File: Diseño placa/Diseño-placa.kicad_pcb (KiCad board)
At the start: 2 copper layers, 57.1 x 44.4 mm, 89 parts, among them IC1 ATMEGA32-P, M1 DIL24, M2 DIL24, M3 DIL16, P1 CONN_01X03, P2 CONN_02X08, P3 CONN_01X01, P4 CONN_01X16, P5 CONN_01X05, P6 CONN_01X05, P7 CONN_02X03, SW1 SW_PUSH, SW2 SW_PUSH, SW3 SW_PUSH, SW4 SW_PUSH, SW5 SW_PUSH, U1 REG104, U2 OPA625, U3 OPA625, U4 OPA625, U5 OPA625, U6 OPA625, U7 OPA625, X1 16M

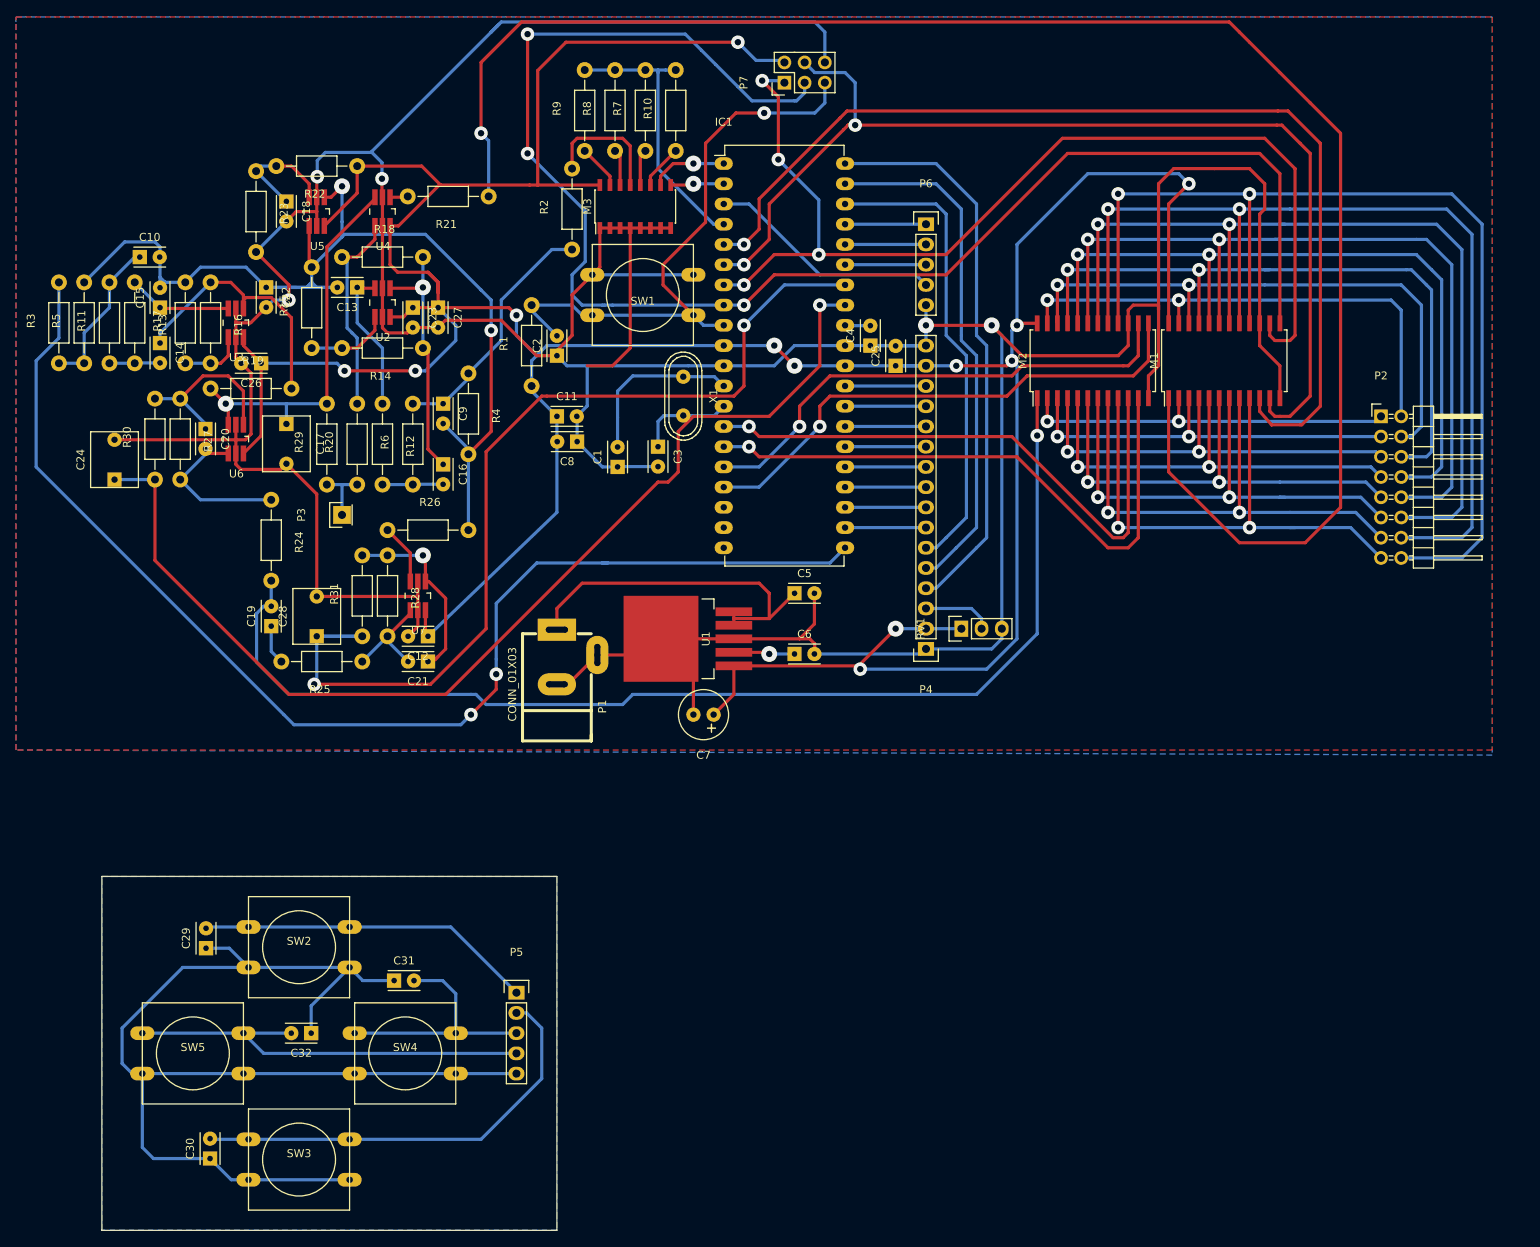
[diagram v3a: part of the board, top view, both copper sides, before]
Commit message: Corrección tamaño de capacitores
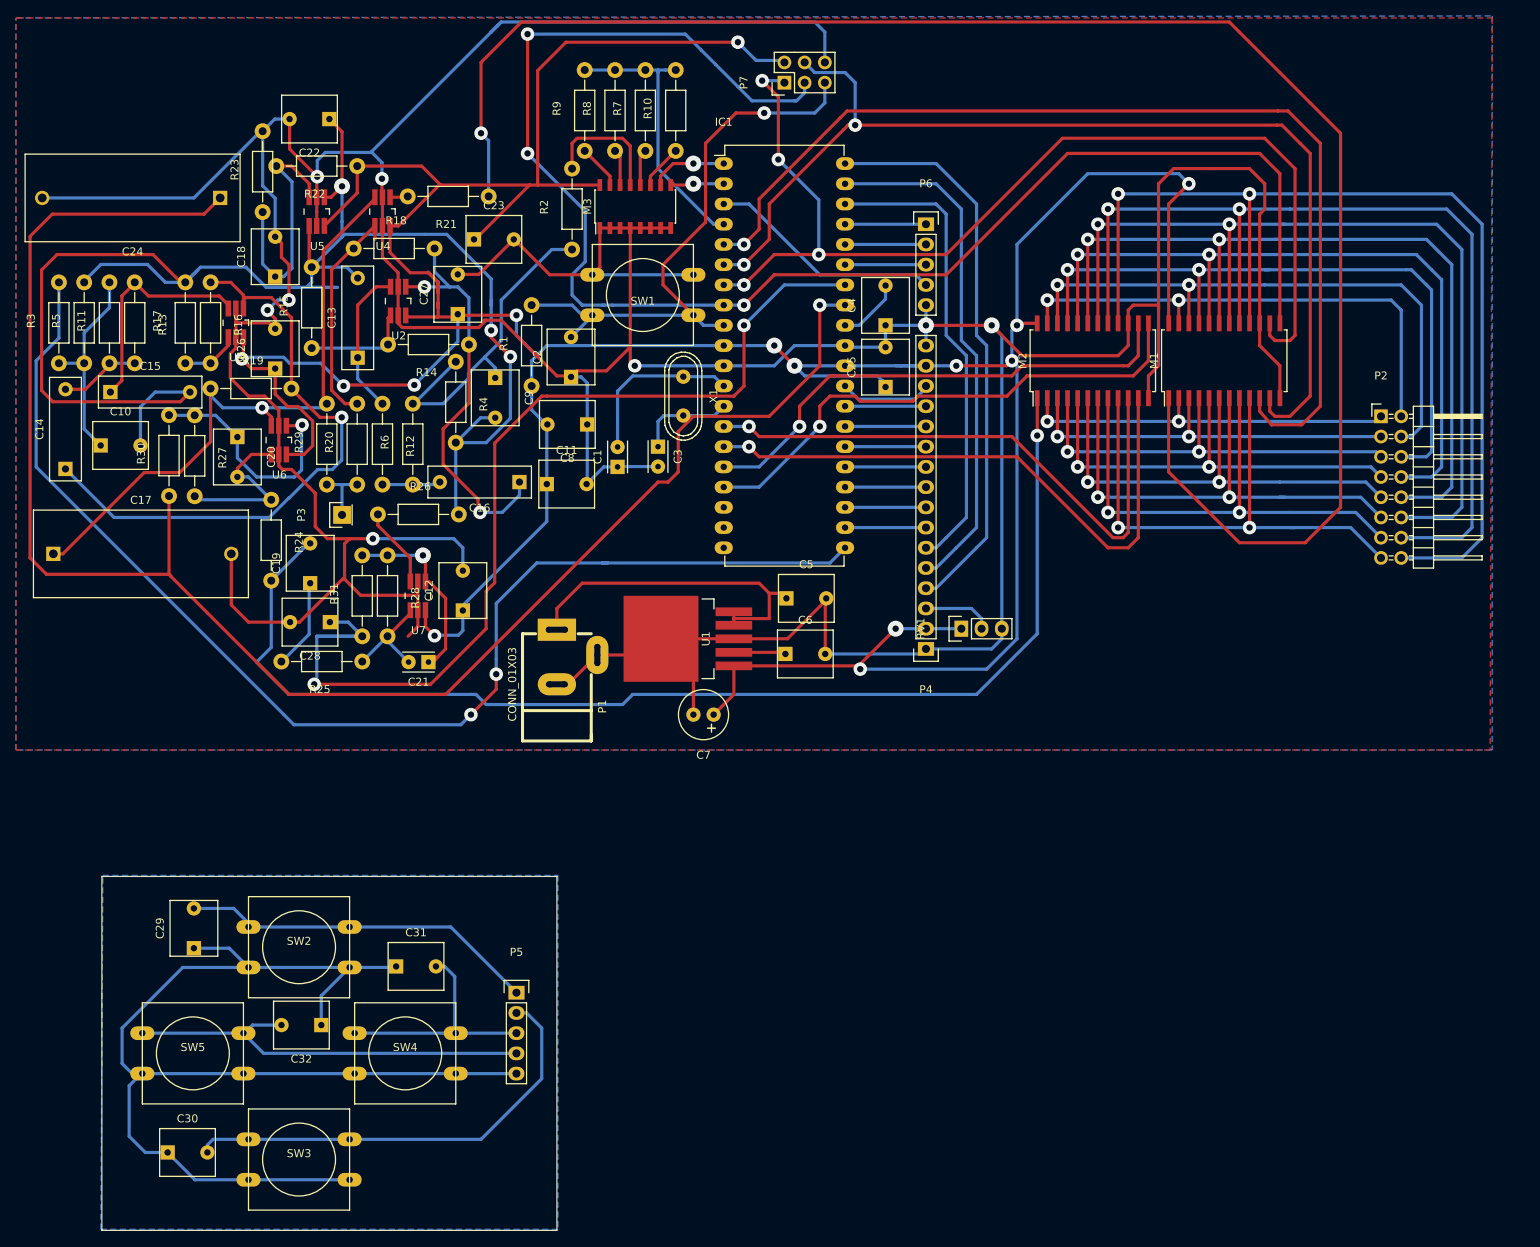
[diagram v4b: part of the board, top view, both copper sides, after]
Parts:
- C10, C11, C12, C18, C19, C2, C20, C22, C23, C25, C26, C27, C29, C30, C31, C32, C4, C5, C6, C8, C9: footprint Capacitors_ThroughHole:C_Rect_L4_W2.5_P2.5 -> Capacitors_ThroughHole:C_Rect_L7_W6_P5
- C13, C14, C15, C16: footprint Capacitors_ThroughHole:C_Rect_L4_W2.5_P2.5 -> Capacitors_ThroughHole:C_Rect_L13_W4_P10
- C17, C24: footprint Capacitors_ThroughHole:C_Rect_L7_W6_P5 -> Capacitors_ThroughHole:C_Rect_L27_W11_P22
- moved C24 37.8 mm to (54.9, 48.8), turned to 180 degrees
- moved C17 33.5 mm to (33.9, 93.5), turned to 0 degrees
- moved C10 24.2 mm to (39.9, 79.9)
- moved C22 22.6 mm to (68.6, 38.9), turned to 180 degrees
- moved C14 19.8 mm to (35.4, 82.8), turned to 90 degrees
- moved C15 12.3 mm to (41.1, 73.2), turned to 0 degrees
- moved C23 11.5 mm to (86.7, 54.0), turned to 0 degrees
- moved C16 9.84 mm to (92.5, 84.5), turned to 180 degrees
- moved C18 9.54 mm to (61.8, 58.6), turned to 90 degrees
- moved C13 8.83 mm to (72.1, 68.8), turned to 90 degrees
- moved C11 8.60 mm to (95.9, 84.7)
- moved C9 7.30 mm to (89.4, 71.4)
- moved C19 7.28 mm to (66.2, 97.2)
- moved R14 5.80 mm to (81.0, 67.2)
- moved C12 5.45 mm to (85.3, 100.6), turned to 90 degrees
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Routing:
- net /VCC/2: track 135.3 -> 217.5 mm, vias 2 -> 3
- net /GND: track 757.8 -> 838.7 mm, vias 5 -> 8
- net /ADCOFFSET: track 136.6 -> 213.3 mm
- net Net-(C14-Pad1): track 33.9 -> 77.0 mm, vias 0 -> 1
- net /VCC: track 456.9 -> 489.7 mm, vias 12 -> 14
- net /OFFSET: track 49.1 -> 80.4 mm
- net Net-(C16-Pad1): track 31.3 -> 51.8 mm, vias 1 -> 2
- net Net-(C18-Pad1): track 14.9 -> 31.7 mm
- net Net-(C15-Pad1): track 13.1 -> 28.4 mm
- net Net-(C9-Pad1): track 31.4 -> 42.1 mm
- net Net-(C20-Pad1): track 22.4 -> 29.5 mm, vias 0 -> 1
- net Net-(C19-Pad1): track 4.97 -> 11.4 mm
- net /MUX1IO: track 145.1 -> 151.3 mm
- net Net-(C10-Pad1): track 19.8 -> 25.8 mm
- net Net-(C4-Pad2): track 3.19 -> 8.20 mm
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
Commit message: Última versión PCB
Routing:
- net /VCC/2: track 217.5 -> 218.5 mm
- net Net-(R14-Pad2): track 13.6 -> 14.2 mm
- net /VCC: track 489.7 -> 490.3 mm
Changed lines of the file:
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@@
     (links 287)
     (no_connects 21)
-    (area 29.109999 25.934999 272.537601 178.485001)
+    (area 29.109999 25.908 272.537601 178.485001)
     (thickness 1.6)
     (drawings 10)
-    (tracks 1118)
+    (tracks 1136)
     (zones 0)
     (modules 89)
@@
   (segment (start 119.38 105.84) (end 125.652 105.84) (width 0.4) (layer F.Cu) (net 7))
   (segment (start 125.652 105.84) (end 125.857 106.045) (width 0.4) (layer F.Cu) (net 7))
+  (segment (start 96.266 67.31) (end 97.028 67.31) (width 0.4) (layer B.Cu) (net 8))
+  (segment (start 100.838 68.072) (end 101.6 67.31) (width 0.4) (layer B.Cu) (net 8))
+  (segment (start 97.79 68.072) (end 100.838 68.072) (width 0.4) (layer B.Cu) (net 8))
+  (segment (start 97.028 67.31) (end 97.79 68.072) (width 0.4) (layer B.Cu) (net 8))
   (segment (start 63.35395 74.97445) (end 64.66205 74.97445) (width 0.4) (layer F.Cu) (net 8))
   (segment (start 64.66205 74.97445) (end 66.4845 76.7969) (width 0.4) (layer F.Cu) (net 8))
@@
   (segment (start 93.98 72.39) (end 93.98 69.215) (width 0.4) (layer B.Cu) (net 8))
   (segment (start 93.98 69.215) (end 94.615 68.58) (width 0.4) (layer B.Cu) (net 8))
-  (segment (start 95.885 67.31) (end 118.11 67.31) (width 0.4) (layer B.Cu) (net 8))
+  (segment (start 95.885 67.31) (end 96.266 67.31) (width 0.4) (layer B.Cu) (net 8))
+  (segment (start 101.6 67.31) (end 118.11 67.31) (width 0.4) (layer B.Cu) (net 8))
   (segment (start 94.615 68.58) (end 95.885 67.31) (width 0.4) (layer B.Cu) (net 8))
   (segment (start 143.51 69.85) (end 139.7 69.85) (width 0.4) (layer B.Cu) (net 8))
@@
   (segment (start 86.0425 70.8025) (end 86.0425 71.4375) (width 0.4) (layer B.Cu) (net 9))
   (segment (start 86.0425 71.4375) (end 82.8675 74.6125) (width 0.4) (layer B.Cu) (net 9))
+  (segment (start 38.354 74.3712) (end 38.8112 74.3712) (width 0.4) (layer F.Cu) (net 10))
+  (segment (start 42.926 75.692) (end 44.2468 74.3712) (width 0.4) (layer F.Cu) (net 10))
+  (segment (start 40.132 75.692) (end 42.926 75.692) (width 0.4) (layer F.Cu) (net 10))
+  (segment (start 38.8112 74.3712) (end 40.132 75.692) (width 0.4) (layer F.Cu) (net 10))
   (segment (start 70.1675 47.3075) (end 70.1675 40.4495) (width 0.4) (layer F.Cu) (net 10))
   (segment (start 70.1675 40.4495) (end 68.58 38.862) (width 0.4) (layer F.Cu) (net 10))
@@
   (segment (start 49.9237 59.3725) (end 46.4312 55.88) (width 0.4) (layer F.Cu) (net 10))
   (segment (start 49.8526 74.3712) (end 51.0718 73.152) (width 0.4) (layer F.Cu) (net 10))
-  (segment (start 33.8582 74.3712) (end 49.8526 74.3712) (width 0.4) (layer F.Cu) (net 10))
+  (segment (start 33.8582 74.3712) (end 38.354 74.3712) (width 0.4) (layer F.Cu) (net 10))
+  (segment (start 44.2468 74.3712) (end 49.8526 74.3712) (width 0.4) (layer F.Cu) (net 10))
   (segment (start 32.4358 72.9488) (end 33.8582 74.3712) (width 0.4) (layer F.Cu) (net 10))
   (segment (start 32.4358 57.8104) (end 32.4358 72.9488) (width 0.4) (layer F.Cu) (net 10))
@@
   (segment (start 78.74254 100.54336) (end 78.74254 100.96246) (width 0.4) (layer F.Cu) (net 25))
   (segment (start 78.74254 100.96246) (end 75.8825 103.8225) (width 0.4) (layer F.Cu) (net 25))
+  (segment (start 123.8885 76.1365) (end 116.6495 76.1365) (width 0.4) (layer F.Cu) (net 26))
+  (segment (start 113.03 77.724) (end 112.395 78.359) (width 0.4) (layer F.Cu) (net 26))
+  (segment (start 115.062 77.724) (end 113.03 77.724) (width 0.4) (layer F.Cu) (net 26))
+  (segment (start 116.6495 76.1365) (end 115.062 77.724) (width 0.4) (layer F.Cu) (net 26))
   (segment (start 48.4378 96.0374) (end 33.0454 96.0374) (width 0.4) (layer F.Cu) (net 26))
   (segment (start 52.832 50.8) (end 54.864 48.768) (width 0.4) (layer F.Cu) (net 26))
@@
   (segment (start 48.6664 96.266) (end 48.6664 96.2914) (width 0.4) (layer F.Cu) (net 26))
   (segment (start 48.4378 96.0374) (end 48.6664 96.266) (width 0.4) (layer F.Cu) (net 26))
-  (segment (start 130.175 62.23) (end 133.35 62.23) (width 0.4) (layer B.Cu) (net 26))
-  (via (at 130.175 62.23) (size 1.7) (drill 0.8) (layers F.Cu B.Cu) (net 26))
-  (segment (start 130.175 69.85) (end 130.175 62.23) (width 0.4) (layer F.Cu) (net 26))
-  (segment (start 123.825 76.2) (end 130.175 69.85) (width 0.4) (layer F.Cu) (net 26))
-  (segment (start 114.3 76.2) (end 123.825 76.2) (width 0.4) (layer F.Cu) (net 26))
-  (segment (start 112.395 78.105) (end 114.3 76.2) (width 0.4) (layer F.Cu) (net 26))
-  (segment (start 112.395 83.185) (end 112.395 78.105) (width 0.4) (layer F.Cu) (net 26))
+  (segment (start 112.395 83.185) (end 112.395 78.359) (width 0.4) (layer F.Cu) (net 26))
   (segment (start 111.125 84.455) (end 112.395 83.185) (width 0.4) (layer F.Cu) (net 26))
   (segment (start 109.855 84.455) (end 111.125 84.455) (width 0.4) (layer F.Cu) (net 26))
@@
   (segment (start 48.6664 96.2914) (end 53.2765 100.9015) (width 0.4) (layer F.Cu) (net 26))
   (segment (start 53.2765 100.9015) (end 63.5 111.125) (width 0.4) (layer F.Cu) (net 26))
+  (segment (start 130.175 62.23) (end 133.35 62.23) (width 0.4) (layer B.Cu) (net 26))
+  (via (at 130.175 62.23) (size 1.7) (drill 0.8) (layers F.Cu B.Cu) (net 26))
+  (segment (start 130.175 69.85) (end 130.175 62.23) (width 0.4) (layer F.Cu) (net 26))
+  (segment (start 123.825 76.2) (end 123.8885 76.1365) (width 0.4) (layer F.Cu) (net 26))
+  (segment (start 123.8885 76.1365) (end 130.175 69.85) (width 0.4) (layer F.Cu) (net 26))
   (segment (start 68.6435 102.0445) (end 70.9295 102.0445) (width 0.4) (layer B.Cu) (net 27))
   (segment (start 70.9295 102.0445) (end 72.7075 103.8225) (width 0.4) (layer B.Cu) (net 27))
@@
   (segment (start 68.2625 84.7725) (end 70.1675 84.7725) (width 0.4) (layer B.Cu) (net 81))
   (segment (start 70.1675 84.7725) (end 72.0725 84.7725) (width 0.4) (layer B.Cu) (net 81))
+  (segment (start 69.85 67.6275) (end 70.0405 67.6275) (width 0.4) (layer B.Cu) (net 82))
+  (segment (start 73.152 66.802) (end 73.9775 67.6275) (width 0.4) (layer B.Cu) (net 82))
+  (segment (start 70.866 66.802) (end 73.152 66.802) (width 0.4) (layer B.Cu) (net 82))
+  (segment (start 70.0405 67.6275) (end 70.866 66.802) (width 0.4) (layer B.Cu) (net 82))
   (segment (start 75.946 67.183) (end 75.946 63.8429) (width 0.4) (layer F.Cu) (net 82))
   (segment (start 75.946 63.8429) (end 76.26604 63.52286) (width 0.4) (layer F.Cu) (net 82))
-  (segment (start 66.3575 67.6275) (end 75.5015 67.6275) (width 0.4) (layer B.Cu) (net 82))
+  (segment (start 66.3575 67.6275) (end 69.85 67.6275) (width 0.4) (layer B.Cu) (net 82))
+  (segment (start 73.9775 67.6275) (end 75.5015 67.6275) (width 0.4) (layer B.Cu) (net 82))
   (segment (start 75.5015 67.6275) (end 75.946 67.183) (width 0.4) (layer B.Cu) (net 82))
   (segment (start 55.88254 66.25336) (end 55.88254 67.30746) (width 0.4) (layer F.Cu) (net 83))
